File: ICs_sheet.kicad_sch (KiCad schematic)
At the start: 38 parts, among them J1 HDR_6_2.54, U1 ESP32-D0WDQ6, U2 TXB0104PWR, U3 IS25WP032D

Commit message: updated ESP32 design - needs silkscreen added and shunt should be moved to be closer to U1
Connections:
- no-connect marks 0 -> 19
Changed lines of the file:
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@@
 		(color 0 0 0 0)
+	)
+	(no_connect
+		(at 68.58 107.95)
+	)
+	(no_connect
+		(at 85.09 119.38)
+	)
+	(no_connect
+		(at 68.58 90.17)
+	)
+	(no_connect
+		(at 68.58 95.25)
+	)
+	(no_connect
+		(at 205.74 49.53)
+	)
+	(no_connect
+		(at 105.41 68.58)
+	)
+	(no_connect
+		(at 68.58 105.41)
+	)
+	(no_connect
+		(at 231.14 49.53)
+	)
+	(no_connect
+		(at 121.92 102.87)
+	)
+	(no_connect
+		(at 107.95 68.58)
+	)
+	(no_connect
+		(at 92.71 68.58)
+	)
+	(no_connect
+		(at 87.63 119.38)
+	)
+	(no_connect
+		(at 68.58 82.55)
+	)
+	(no_connect
+		(at 68.58 92.71)
+	)
+	(no_connect
+		(at 90.17 119.38)
+	)
+	(no_connect
+		(at 68.58 97.79)
+	)
+	(no_connect
+		(at 68.58 102.87)
+	)
+	(no_connect
+		(at 97.79 68.58)
+	)
+	(no_connect
+		(at 82.55 119.38)
 	)
 	(wire

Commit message: updated design - removed visible pin numbers from passives, fixed connections, updated silkscreen
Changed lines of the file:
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@@
 	(wire
 		(pts
-			(xy 209.55 116.84) (xy 219.71 116.84)
+			(xy 209.55 116.84) (xy 220.98 116.84)
 		)
 		(stroke
@@
 	(wire
 		(pts
-			(xy 52.07 93.98) (xy 48.26 93.98)
+			(xy 49.53 93.98) (xy 46.99 93.98)
 		)
 		(stroke
@@
 	(wire
 		(pts
-			(xy 240.03 116.84) (xy 229.87 116.84)
+			(xy 240.03 116.84) (xy 228.6 116.84)
 		)
 		(stroke
@@
 	(wire
 		(pts
+			(xy 59.69 93.98) (xy 57.15 93.98)
+		)
+		(stroke
+			(width 0)
+			(type default)
+		)
+	)
+	(wire
+		(pts
 			(xy 90.17 45.72) (xy 90.17 55.88)
 		)
@@
 	(wire
 		(pts
-			(xy 209.55 97.79) (xy 209.55 102.87)
-		)
-		(stroke
-			(width 0)
-			(type default)
-		)
-	)
-	(wire
-		(pts
 			(xy 240.03 102.87) (xy 240.03 107.95)
 		)
@@
 	(wire
 		(pts
+			(xy 209.55 96.52) (xy 209.55 102.87)
+		)
+		(stroke
+			(width 0)
+			(type default)
+		)
+	)
+	(wire
+		(pts
 			(xy 231.14 52.07) (xy 240.03 52.07)
 		)
@@
 	(wire
 		(pts
-			(xy 243.84 105.41) (xy 246.38 105.41)
+			(xy 209.55 82.55) (xy 209.55 88.9)
 		)
 		(stroke
@@
 	(wire
 		(pts
-			(xy 121.92 87.63) (xy 144.78 87.63)
+			(xy 243.84 105.41) (xy 246.38 105.41)
 		)
 		(stroke
@@
 	(wire
 		(pts
-			(xy 273.05 105.41) (xy 273.05 110.49)
+			(xy 121.92 87.63) (xy 144.78 87.63)
 		)
 		(stroke
@@
 	(wire
 		(pts
-			(xy 209.55 82.55) (xy 209.55 87.63)
+			(xy 273.05 105.41) (xy 273.05 110.49)
 		)
 		(stroke
@@
 	(symbol
 		(lib_id "power:VCC")
-		(at 48.26 93.98 0)
+		(at 46.99 93.98 0)
 		(unit 1)
 		(exclude_from_sim no)
@@
 		(dnp no)
 		(property "Reference" "#PWR042"
-			(at 48.26 97.79 0)
+			(at 46.99 97.79 0)
 			(effects
 				(font
@@
 		)
 		(property "Value" "VCC"
-			(at 48.26 90.17 0)
+			(at 46.99 90.17 0)
 			(effects
 				(font
@@
 		)
 		(property "Footprint" ""
-			(at 48.26 93.98 0)
+			(at 46.99 93.98 0)
 			(effects
 				(font
@@
 		)
 		(property "Datasheet" ""
-			(at 48.26 93.98 0)
+			(at 46.99 93.98 0)
 			(effects
 				(font
@@
 		)
 		(property "Description" "Power symbol creates a global label with name \"VCC\""
-			(at 48.26 93.98 0)
+			(at 46.99 93.98 0)
 			(effects
 				(font
@@
 	(symbol
 		(lib_id "0603_Yageo_Res:RES_10k_0603")
-		(at 55.88 93.98 0)
+		(at 53.34 93.98 0)
 		(mirror x)
 		(unit 1)
@@
 		(dnp no)
 		(property "Reference" "R6"
-			(at 57.15 91.948 0)
+			(at 54.61 91.948 0)
 			(effects
 				(font
@@
 		)
 		(property "Value" "RES_10k_0603"
-			(at 67.31 22.86 0)
+			(at 64.77 22.86 0)
 			(effects
 				(font
@@
 		)
 		(property "Footprint" "Resistor_SMD:R_0603_1608Metric"
-			(at 55.88 26.67 0)
+			(at 53.34 26.67 0)
 			(effects
 				(font
@@
 		)
 		(property "Datasheet" "https://www.yageo.com/upload/media/product/products/datasheet/rchip/PYu-RC_Group_51_RoHS_L_12.pdf"
-			(at 86.36 31.75 0)
+			(at 83.82 31.75 0)
 			(effects
 				(font
@@
 		)
 		(property "Description" "RES 10K OHM 1% 1/10W 0603"
-			(at 76.2 34.29 0)
+			(at 73.66 34.29 0)
 			(effects
 				(font
@@
 		)
 		(property "Display Value" "10k"
-			(at 57.658 96.266 0)
+			(at 55.118 96.266 0)
 			(effects
 				(font
@@
 		)
 		(property "Manufacturer" "YAGEO"
-			(at 46.99 22.86 0)
+			(at 44.45 22.86 0)
 			(effects
 				(font
@@
 		)
 		(property "Manufacturer Part Number" "RC0603FR-0710KL"
-			(at 45.72 29.21 0)
+			(at 43.18 29.21 0)
 			(effects
 				(font
@@
 		)
 		(property "Supplier 1" "DigiKey"
-			(at 40.64 20.32 0)
+			(at 38.1 20.32 0)
 			(effects
 				(font
@@
 		)
 		(property "Supplier 1 Part Number" "311-10.0KHRCT-ND"
-			(at 68.58 20.32 0)
+			(at 66.04 20.32 0)
 			(effects
 				(font
@@
 		)
 		(property "Supplier 2" "no_data"
-			(at 55.245 90.805 0)
+			(at 52.705 90.805 0)
 			(effects
 				(font
@@
 		)
 		(property "Supplier 2 Part Number" "no_data"
-			(at 55.245 88.265 0)
+			(at 52.705 88.265 0)
 			(effects
 				(font

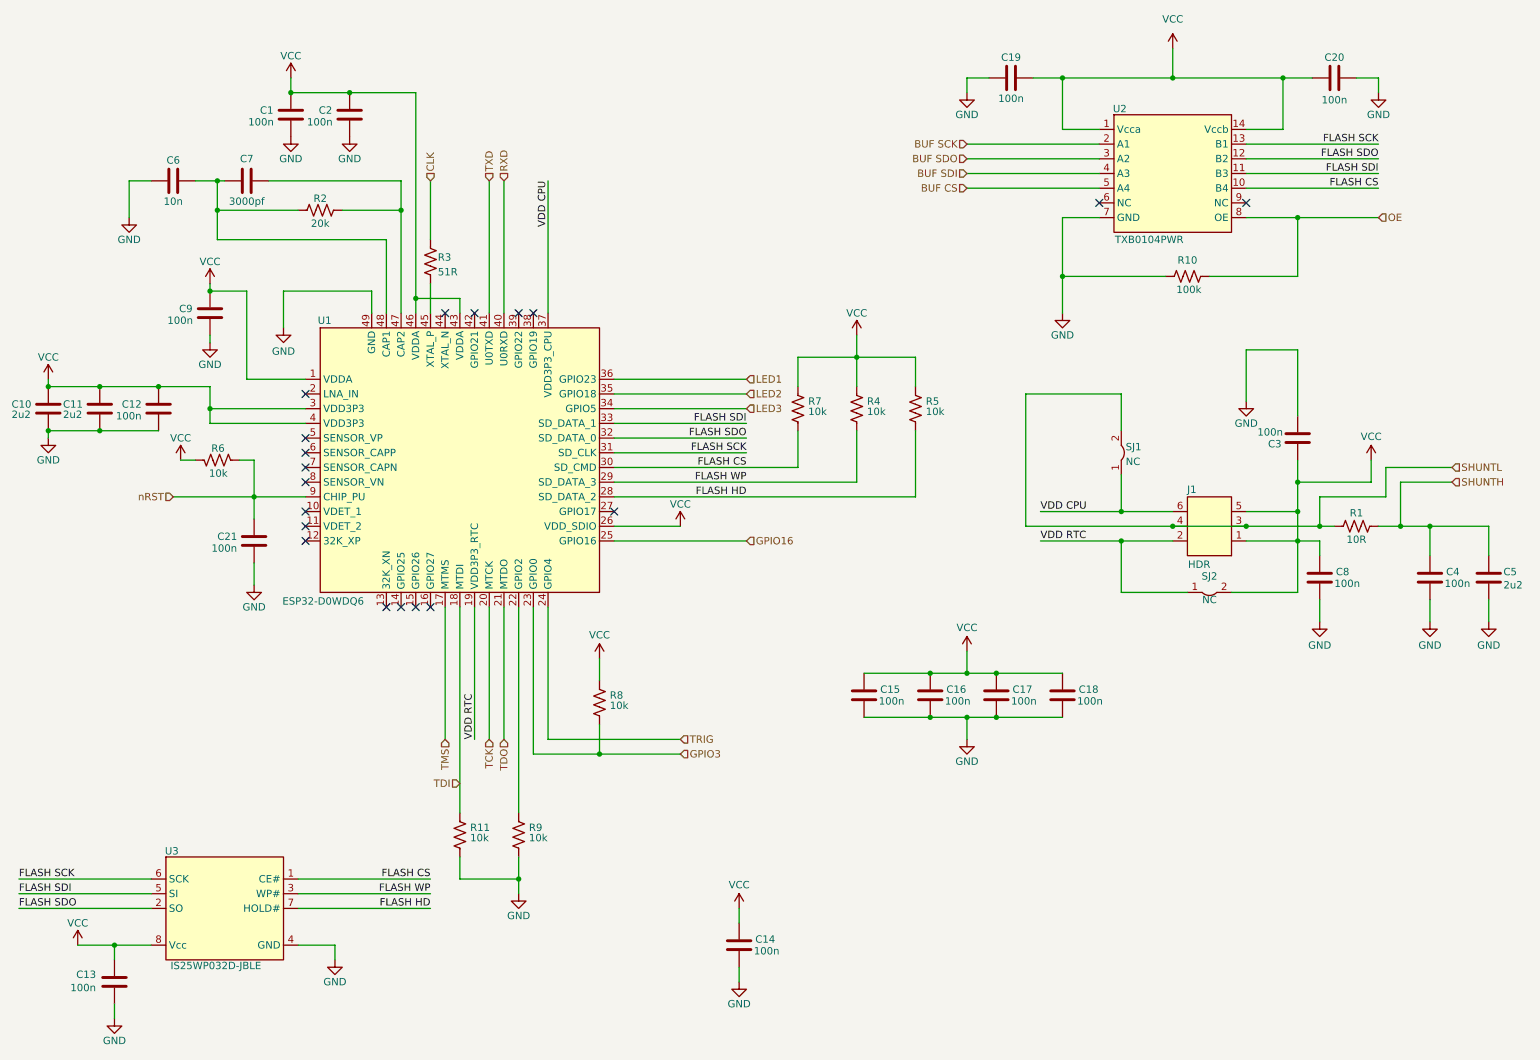
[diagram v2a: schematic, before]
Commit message: updated pcb and schematic after library re-organization, also updated header to the correct footprint
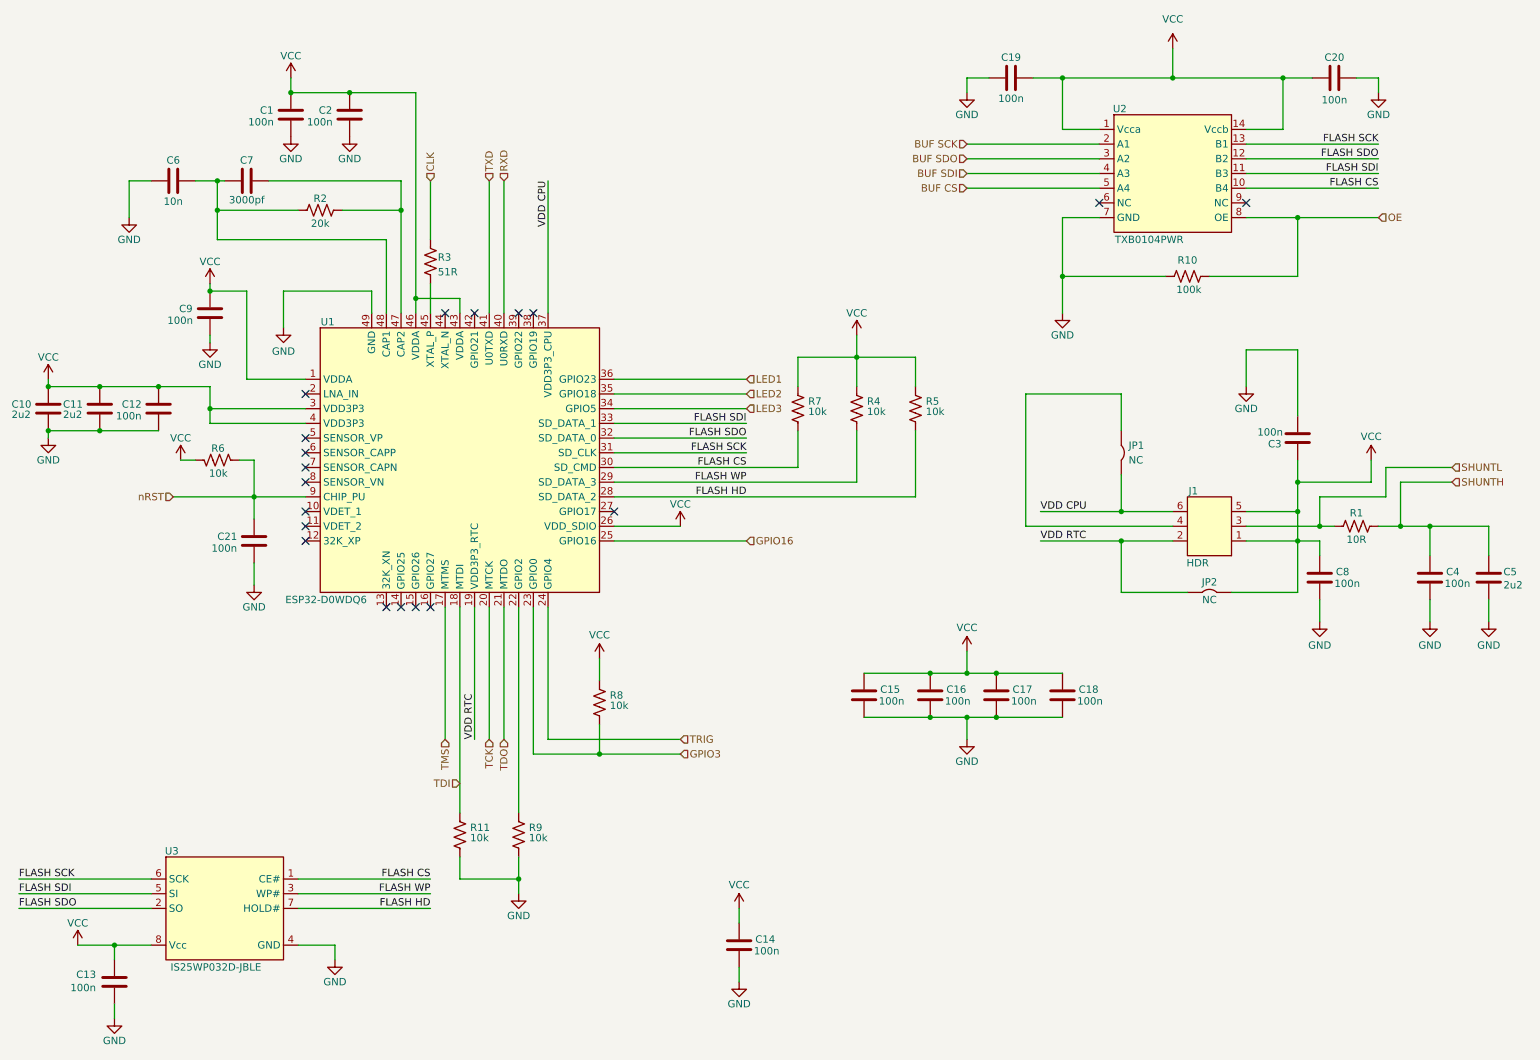
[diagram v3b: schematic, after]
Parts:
- removed C7: CAP_3000p_50V_0603, Capacitor_SMD:C_0603_1608Metric, symbol tutorial_2_library:CAP_3000p_50V_0603
- removed J1: HDR_6_2.54, Connector_PinHeader_1.00mm:PinHeader_2x03_P1.00mm_Vertical, symbol tutorial_2_library:VERT_HDR_6_2.54mm
- removed SJ1, SJ2: ~, Jumper:SolderJumper-2_P1.3mm_Bridged2Bar_Pad1.0x1.5mm, symbol tutorial_2_library:Solder_Jumper_2_NC
- removed U1: ESP32-D0WDQ6, Package_DFN_QFN:QFN-48-1EP_6x6mm_P0.4mm_EP4.3x4.3mm, symbol tutorial_2_library:ESP32-D0WDQ6
- removed U2: TXB0104PWR, Package_SO:SOIC-14_3.9x8.7mm_P1.27mm, symbol tutorial_2_library:TXB0104PWR
- removed U3: IS25WP032D, Package_SO:SOIC-8_5.275x5.275mm_P1.27mm, symbol tutorial_2_library:IS25WP032D-JBLE
- added C7: CAP_3000p_50V_0603, Capacitor_SMD:C_0603_1608Metric, symbol nae_caps:CAP_3000p_50V_0603
- added J1: HDR_6_2.54, Connector_PinHeader_2.54mm:PinHeader_2x03_P2.54mm_Vertical, symbol NAE_Connectors:VERT_HDR_2x3_2.54mm
- added JP1, JP2: ~, Jumper:SolderJumper-2_P1.3mm_Bridged2Bar_Pad1.0x1.5mm, symbol NAE_Connectors:Solder_Jumper_2_NC
- added U1: ESP32-D0WDQ6, Package_DFN_QFN:QFN-48-1EP_6x6mm_P0.4mm_EP4.3x4.3mm, symbol NAE_Integrated_Circuits:ESP32-D0WDQ6
- added U2: TXB0104PWR, Package_SO:SOIC-14_3.9x8.7mm_P1.27mm, symbol NAE_Integrated_Circuits:TXB0104PWR
- added U3: IS25WP032D, Package_SO:SOIC-8_5.275x5.275mm_P1.27mm, symbol NAE_Integrated_Circuits:IS25WP032D-JBLE
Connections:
- net BUF CS: now also U2.5 (A4)
- net BUF SCK: now also U2.2 (A1)
- net BUF SDI: now also U2.4 (A3)
- net BUF SDO: now also U2.3 (A2)
- net FLASH CS: now also U1.30 (SD_CMD), U2.10 (B4), U3.1 (CE#)
- net FLASH HD: now also U1.28 (SD_DATA_2), U3.7 (HOLD#)
- net FLASH SCK: now also U1.31 (SD_CLK), U2.13 (B1), U3.6 (SCK)
- net FLASH SDI: now also U1.33 (SD_DATA_1), U2.11 (B3), U3.5 (SI)
- net FLASH SDO: now also U1.32 (SD_DATA_0), U2.12 (B2), U3.2 (SO)
- net FLASH WP: now also U1.29 (SD_DATA_3), U3.3 (WP#)
- net GND: now also U1.49 (GND), U2.7 (GND), U3.4 (GND)
- net GPIO16: now also U1.25 (GPIO16)
- net GPIO3: now also U1.23 (GPIO0)
- net LED1: now also U1.36 (GPIO23)
- net LED2: now also U1.35 (GPIO18)
- net LED3: now also U1.34 (GPIO5)
- net OE: now also U2.8 (OE)
- net RXD: now also U1.40 (U0RXD)
- net SHUNTL: now also J1.3
- net TCK: now also U1.20 (MTCK)
- net TDI: now also U1.18 (MTDI)
- net TDO: now also U1.21 (MTDO)
- net TMS: now also U1.17 (MTMS)
- net TRIG: now also U1.24 (GPIO4)
- net TXD: now also U1.41 (U0TXD)
- net VCC: now also J1.1, J1.5, JP2.1, U1.1 (VDDA), U1.26 (VDD_SDIO), U1.3 (VDD3P3), U1.4 (VDD3P3), U1.43 (VDDA), U1.46 (VDDA), U2.1 (Vcca), U2.14 (Vccb), U3.8 (Vcc)
- net VDD CPU: now also J1.6, JP1.1, U1.37 (VDD3P3_CPU)
- net VDD RTC: now also J1.2, JP2.2, U1.19 (VDD3P3_RTC)
- net nRST: now also U1.9 (CHIP_PU)
- net at C6.2, R2.1: now also C7.1, U1.48 (CAP1)
- net at R2.2: now also C7.2, U1.47 (CAP2)
- net at R9.2: now also U1.22 (GPIO2)
- net at R3.1: now also U1.45 (XTAL_P)
- new net: J1.4, JP1.2
